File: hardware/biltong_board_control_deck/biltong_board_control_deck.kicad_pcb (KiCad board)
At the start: 2 copper layers, 100 x 70 mm, 32 parts, among them J1 SH1122_DISP, J2 BILTONG_BOARD, Q1 MMBT3904, SW1 UP, SW2 ENTER, SW3 DOWN

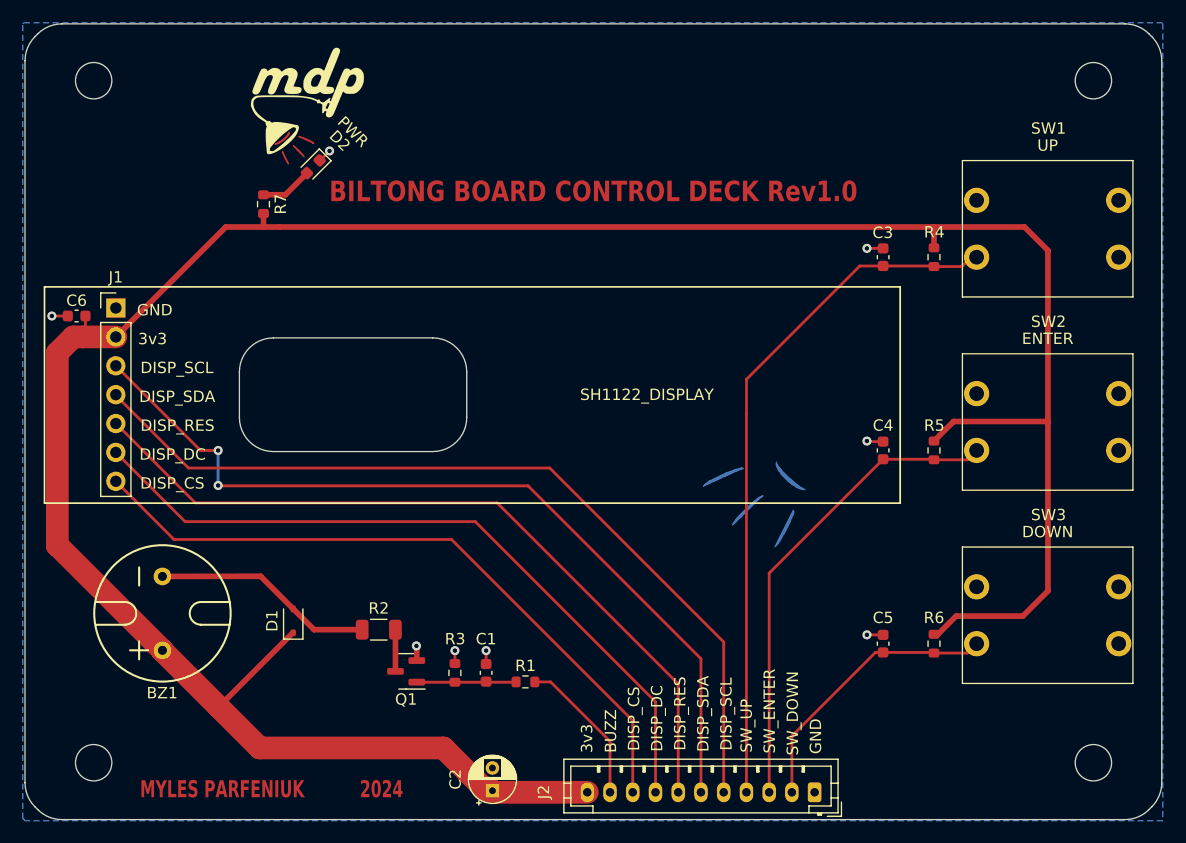
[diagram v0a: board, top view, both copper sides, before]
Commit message: generated BOM, swapped 10u cap size, README.md changes
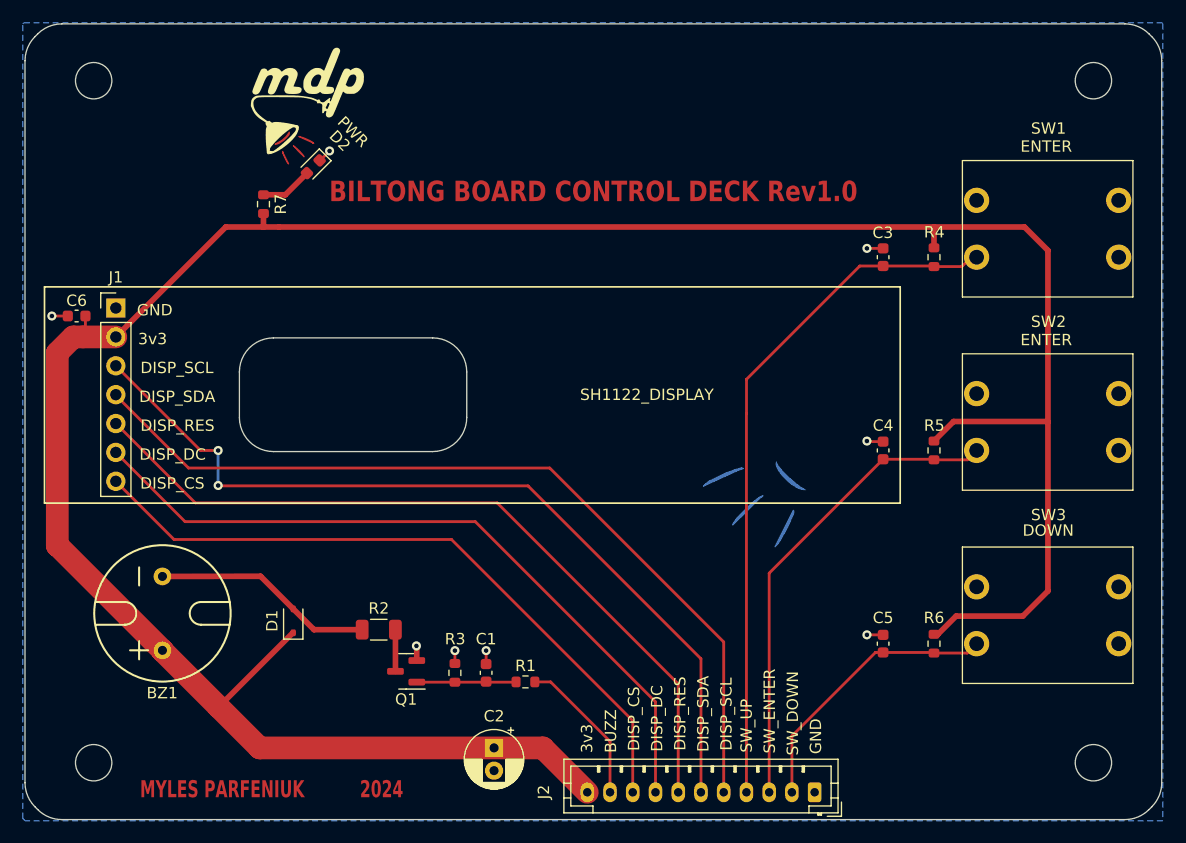
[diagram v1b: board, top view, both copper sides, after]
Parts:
- BZ1: value Buzzer -> GT-111P
- C2: footprint Capacitor_THT:CP_Radial_D4.0mm_P2.00mm -> Capacitor_THT:CP_Radial_D5.0mm_P2.00mm
- J2: value BILTONG_BOARD -> JST_PH_B11B-PH-K_1x11
- SW1: value UP -> TS14-1212-150-BK-260-SCR-D
- SW2: value ENTER -> TS14-1212-150-BK-260-SCR-D
- SW3: value DOWN -> TS14-1212-150-BK-260-SCR-D
- moved C2 3.77 mm to (140.5, 107.7), turned to -90 degrees
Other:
- board text added: "DOWN"
- board text added: "ENTER"

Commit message: corrected control deck schematic values
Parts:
- D1: value D_Schottky -> SD101AWS-TP
- D2: value LED -> 150060VS7500
- J1: value SH1122_DISP -> PinHeader_1x07_P2.54mm_Vertical
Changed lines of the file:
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@@
         (effects (font (size 1 1) (thickness 0.16)))
     )
-    (fp_text value "SH1122_DISP" (at 0.112 -4.74) (layer "F.Fab")
+    (fp_text value "PinHeader_1x07_P2.54mm_Vertical" (at 5.79 -4.18) (layer "F.Fab")
         (effects (font (size 1 1) (thickness 0.15)))
     )
@@
         (effects (font (size 1 1) (thickness 0.16)))
     )
-    (fp_text value "GT-111P" (at 0 7.366 90 unlocked) (layer "F.Fab")
+    (fp_text value "GT-111P" (at 0.15 -7.28 90 unlocked) (layer "F.Fab")
         (effects (font (size 1 1) (thickness 0.15)))
     )
@@
         (effects (font (size 1 1) (thickness 0.16)))
     )
-    (fp_text value "D_Schottky" (at -2.912 -0.026 180) (layer "F.Fab")
+    (fp_text value "SD101AWS-TP" (at -2.702 -0.236 180) (layer "F.Fab")
         (effects (font (size 1 1) (thickness 0.15)))
     )
@@
         (effects (font (size 1 1) (thickness 0.16)))
     )
-    (fp_text value "LED" (at 0 1.43 45) (layer "F.Fab")
+    (fp_text value "150060VS7500" (at 0 1.43 45) (layer "F.Fab")
         (effects (font (size 1 1) (thickness 0.15)))
     )

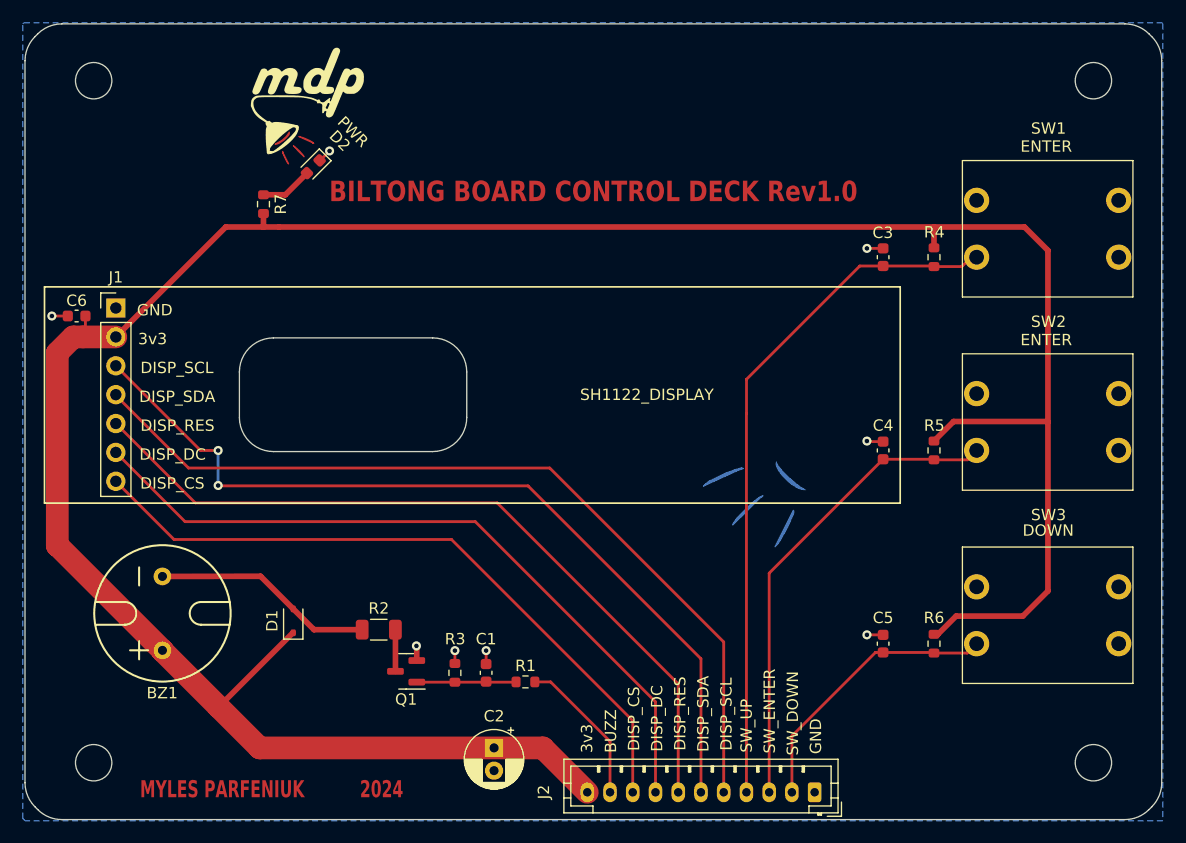
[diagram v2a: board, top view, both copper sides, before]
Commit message: Generated gerbers, moved cap trace, cleaned up buck fills
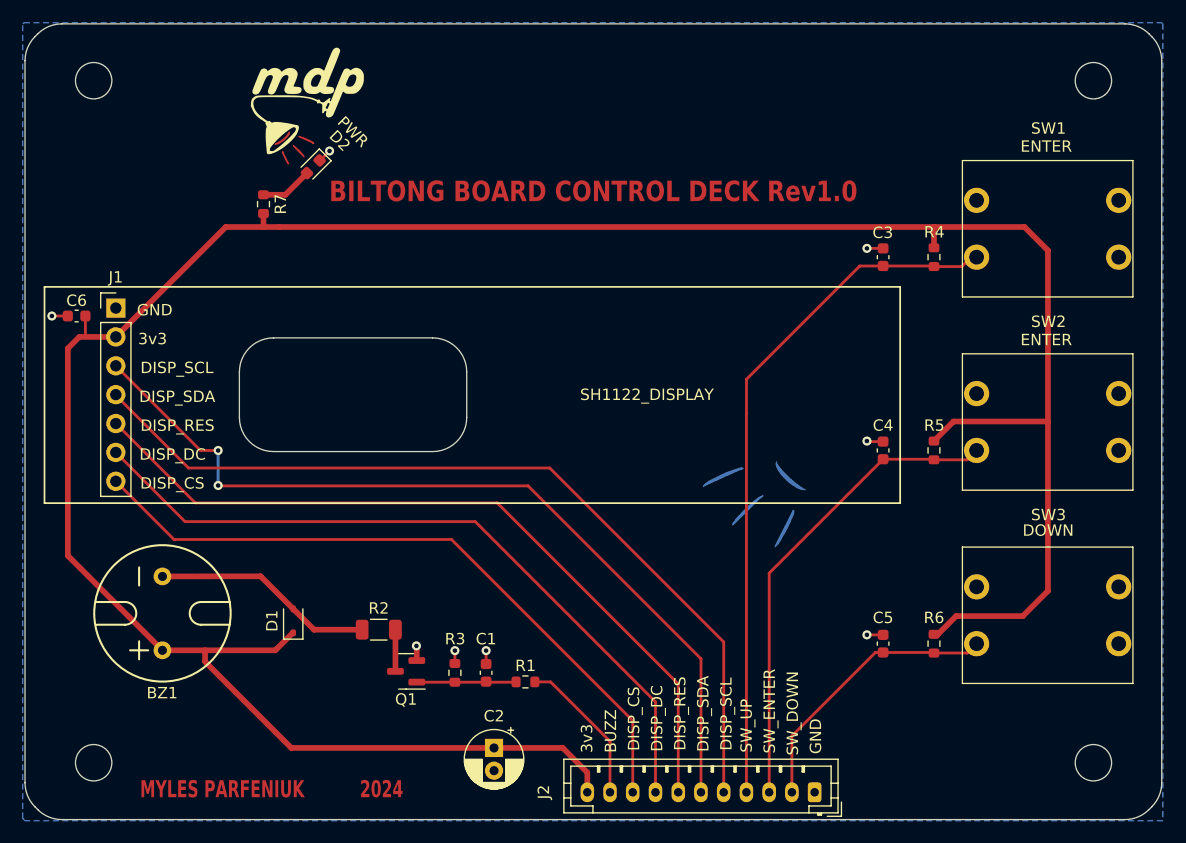
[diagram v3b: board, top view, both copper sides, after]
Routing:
- net +3V3: track 231.7 -> 231.0 mm
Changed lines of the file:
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@@
     (pad_to_mask_clearance 0)
     (pcbplotparams
-      (layerselection 0x00010fc_ffffffff)
+      (layerselection 0x00010c0_ffffffff)
       (plot_on_all_layers_selection 0x0000000_00000000)
       (disableapertmacros false)
-      (usegerberextensions false)
-      (usegerberattributes true)
-      (usegerberadvancedattributes true)
-      (creategerberjobfile true)
+      (usegerberextensions true)
+      (usegerberattributes false)
+      (usegerberadvancedattributes false)
+      (creategerberjobfile false)
       (dashed_line_dash_ratio 12.000000)
       (dashed_line_gap_ratio 3.000000)
@@
       (outputformat 1)
       (mirror false)
-      (drillshape 1)
+      (drillshape 0)
       (scaleselection 1)
-      (outputdirectory "")
+      (outputdirectory "gerbers/")
     )
   )
@@
     (fp_line (start 1.6 0.8) (end -1.6 0.8)
       (stroke (width 0.1) (type solid)) (layer "F.Fab"))
-    (pad "1" smd roundrect (at -1.4625 0 180) (size 1.125 1.75) (layers "F.Cu" "F.Paste" "F.Mask") (roundrect_rratio 0.222222)
+    (pad "1" smd roundrect (at -1.4625 0 180) (size 1.125 1.75) (layers "F.Cu" "F.Paste" "F.Mask") (roundrect_rratio 0.2222222222)
       (net 14 "Net-(Q1-C)") (pintype "passive"))
-    (pad "2" smd roundrect (at 1.4625 0 180) (size 1.125 1.75) (layers "F.Cu" "F.Paste" "F.Mask") (roundrect_rratio 0.222222)
+    (pad "2" smd roundrect (at 1.4625 0 180) (size 1.125 1.75) (layers "F.Cu" "F.Paste" "F.Mask") (roundrect_rratio 0.2222222222)
       (net 2 "Net-(BZ1-+)") (pintype "passive"))
     (model "${KICAD6_3DMODEL_DIR}/Resistor_SMD.3dshapes/R_1206_3216Metric.wrl"
@@
     (fp_line (start 21.95 2.8) (end 21.95 -1.7)
       (stroke (width 0.1) (type solid)) (layer "F.Fab"))
-    (pad "1" thru_hole roundrect (at 0 0 180) (size 1.2 1.75) (drill 0.75) (layers "*.Cu" "*.Mask") (roundrect_rratio 0.208333)
+    (pad "1" thru_hole roundrect (at 0 0 180) (size 1.2 1.75) (drill 0.75) (layers "*.Cu" "*.Mask") (roundrect_rratio 0.2083333333)
       (net 4 "GND") (pinfunction "Pin_1") (pintype "passive") (zone_connect 2))
     (pad "2" thru_hole oval (at 2 0 180) (size 1.2 1.75) (drill 0.75) (layers "*.Cu" "*.Mask")
@@
     (style (thickness 0.1) (arrow_length 1.27) (text_position_mode 0) (extension_height 0.58642) (extension_offset 0.5) keep_text_aligned)
   )
-  (segment (start 111.29 99.11) (end 111.29 99.145786) (width 2) (layer "F.Cu") (net 1))
   (segment (start 120.18 60.685) (end 120.18 61.86) (width 0.5) (layer "F.Cu") (net 1))
-  (segment (start 144.761 107.696) (end 119.844214 107.696) (width 2) (layer "F.Cu") (net 1))
-  (segment (start 111.29 99.145786) (end 116.237107 104.092893) (width 2) (layer "F.Cu") (net 1))
   (segment (start 189.19 79) (end 189.18 79.01) (width 0.5) (layer "F.Cu") (net 1))
+  (segment (start 140.462 107.696) (end 122.626 107.696) (width 0.5) (layer "F.Cu") (net 1))
   (segment (start 179.165 80.7) (end 180.885 78.98) (width 0.5) (layer "F.Cu") (net 1))
   (segment (start 181.11 96.1) (end 186.98 96.1) (width 0.5) (layer "F.Cu") (net 1))
-  (segment (start 102.04 89.895785) (end 102.075785 89.895785) (width 2) (layer "F.Cu") (net 1))
+  (segment (start 122.762 97.568) (end 121.34 98.99) (width 0.5) (layer "F.Cu") (net 1))
+  (segment (start 102.97 90.79) (end 111.29 99.11) (width 0.5) (layer "F.Cu") (net 1))
   (segment (start 122.796 97.568) (end 122.762 97.568) (width 0.5) (layer "F.Cu") (net 1))
   (segment (start 121.526 61.87) (end 120.17 61.87) (width 0.5) (layer "F.Cu") (net 1))
-  (segment (start 102.04 72.95) (end 102.04 89.895785) (width 2) (layer "F.Cu") (net 1))
+  (segment (start 107.19 71.54) (end 103.98 71.54) (width 0.5) (layer "F.Cu") (net 1))
   (segment (start 186.98 96.1) (end 189.19 93.89) (width 0.5) (layer "F.Cu") (net 1))
-  (segment (start 122.762 97.568) (end 116.237107 104.092893) (width 0.5) (layer "F.Cu") (net 1))
+  (segment (start 122.626 107.696) (end 115.04 100.11) (width 0.5) (layer "F.Cu") (net 1))
+  (segment (start 116.39 99.11) (end 121.22 99.11) (width 0.5) (layer "F.Cu") (net 1))
   (segment (start 116.86 61.87) (end 107.19 71.54) (width 0.5) (layer "F.Cu") (net 1))
-  (segment (start 104.3 71.54) (end 107.19 71.54) (width 2) (layer "F.Cu") (net 1))
-  (segment (start 104.3 71.54) (end 103.45 71.54) (width 2) (layer "F.Cu") (net 1))
+  (segment (start 148.665 111.6) (end 148.665 109.855) (width 0.5) (layer "F.Cu") (net 1))
+  (segment (start 148.665 109.855) (end 146.506 107.696) (width 0.5) (layer "F.Cu") (net 1))
   (segment (start 189.19 93.89) (end 189.19 63.93) (width 0.5) (layer "F.Cu") (net 1))
+  (segment (start 102.97 72.55) (end 102.97 90.79) (width 0.5) (layer "F.Cu") (net 1))
+  (segment (start 103.98 71.54) (end 102.97 72.55) (width 0.5) (layer "F.Cu") (net 1))
   (segment (start 189.17 78.98) (end 189.19 79) (width 0.5) (layer "F.Cu") (net 1))
+  (segment (start 146.506 107.696) (end 140.462 107.696) (width 0.5) (layer "F.Cu") (net 1))
   (segment (start 120.17 61.87) (end 116.86 61.87) (width 0.5) (layer "F.Cu") (net 1))
-  (segment (start 103.45 71.54) (end 102.04 72.95) (width 2) (layer "F.Cu") (net 1))
-  (segment (start 119.844214 107.7) (end 116.237107 104.092893) (width 2) (layer "F.Cu") (net 1))
-  (segment (start 148.665 111.6) (end 144.761 107.696) (width 2) (layer "F.Cu") (net 1))
-  (segment (start 102.075785 89.895785) (end 111.29 99.11) (width 2) (layer "F.Cu") (net 1))
+  (segment (start 115.04 100.11) (end 115.04 99.11) (width 0.5) (layer "F.Cu") (net 1))
+  (segment (start 121.22 99.11) (end 121.34 98.99) (width 0.5) (layer "F.Cu") (net 1))
   (segment (start 189.19 63.93) (end 187.13 61.87) (width 0.5) (layer "F.Cu") (net 1))
   (segment (start 179.165 61.895) (end 179.19 61.87) (width 0.5) (layer "F.Cu") (net 1))
@@
   (segment (start 179.19 61.87) (end 121.526 61.87) (width 0.5) (layer "F.Cu") (net 1))
   (segment (start 187.13 61.87) (end 179.19 61.87) (width 0.5) (layer "F.Cu") (net 1))
-  (segment (start 104.3 71.54) (end 104.29 71.53) (width 0.25) (layer "F.Cu") (net 1))
   (segment (start 180.885 78.98) (end 189.17 78.98) (width 0.5) (layer "F.Cu") (net 1))
   (segment (start 179.51 97.7) (end 181.11 96.1) (width 0.5) (layer "F.Cu") (net 1))
-  (segment (start 104.3 71.54) (end 104.515 71.325) (width 0.25) (layer "F.Cu") (net 1))
   (segment (start 120.18 61.86) (end 120.17 61.87) (width 0.5) (layer "F.Cu") (net 1))
   (segment (start 179.165 63.7) (end 179.165 61.895) (width 0.5) (layer "F.Cu") (net 1))
+  (segment (start 111.29 99.11) (end 116.39 99.11) (width 0.5) (layer "F.Cu") (net 1))
   (segment (start 104.515 71.325) (end 104.515 69.7) (width 0.25) (layer "F.Cu") (net 1))
   (segment (start 119.923785 92.595785) (end 122.796 95.468) (width 0.5) (layer "F.Cu") (net 2))
